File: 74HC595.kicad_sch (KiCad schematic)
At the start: 17 parts, among them J1 Conn_01x02_Female, J2 Conn_01x07_Female, Q1 BC547, U1 74HC595, U2 NE555P

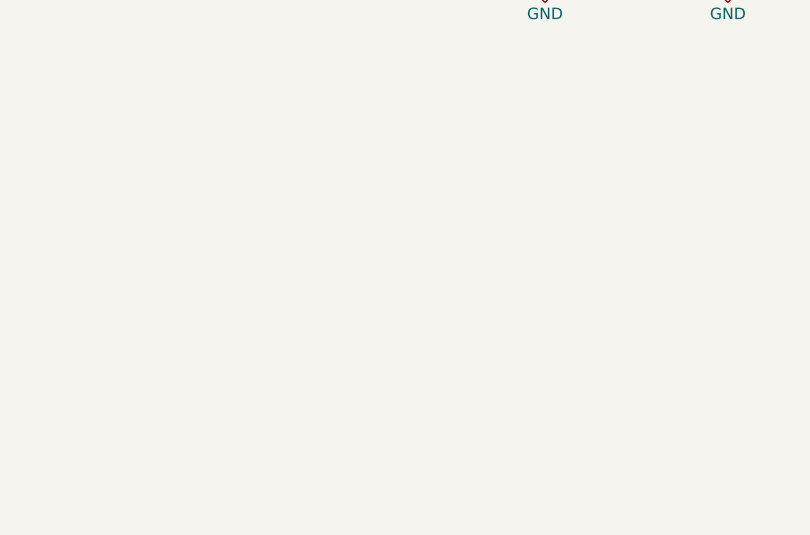
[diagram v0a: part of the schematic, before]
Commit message: schematic update
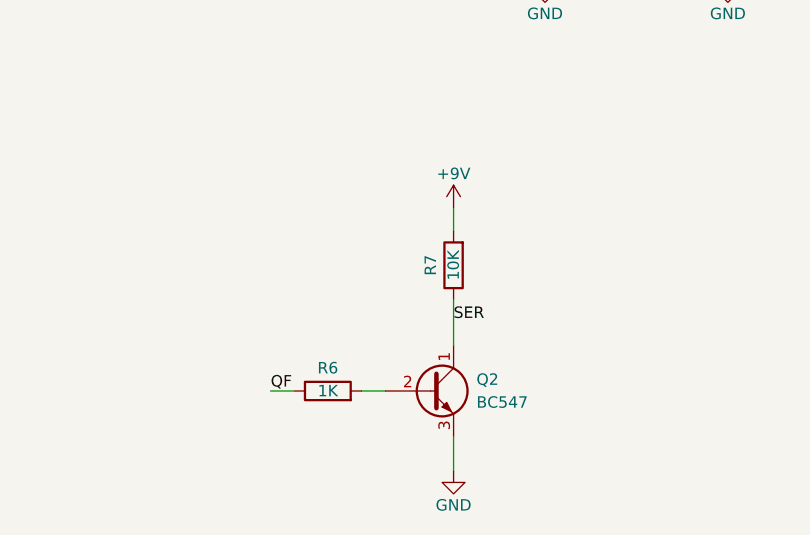
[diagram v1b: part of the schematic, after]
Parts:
- added Q2: BC547, Package_TO_SOT_THT:TO-92_Inline, symbol Transistor_BJT:BC547
- added R6: 1K, Resistor_THT:R_Axial_DIN0207_L6.3mm_D2.5mm_P7.62mm_Horizontal, symbol Device:R
- added R7: 10K, Resistor_THT:R_Axial_DIN0207_L6.3mm_D2.5mm_P7.62mm_Horizontal, symbol Device:R
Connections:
- net +9V: now also R7.2
- net GND: now also Q2.3 (E)
- net QF: now also R6.1
- net SER: now also Q2.1 (C), R7.1
- new net: Q2.2 (B), R6.2
